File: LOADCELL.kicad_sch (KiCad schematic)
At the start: 11 parts, among them J18 Conn_01x04_Socket, Q4 S8550, U1 HX711

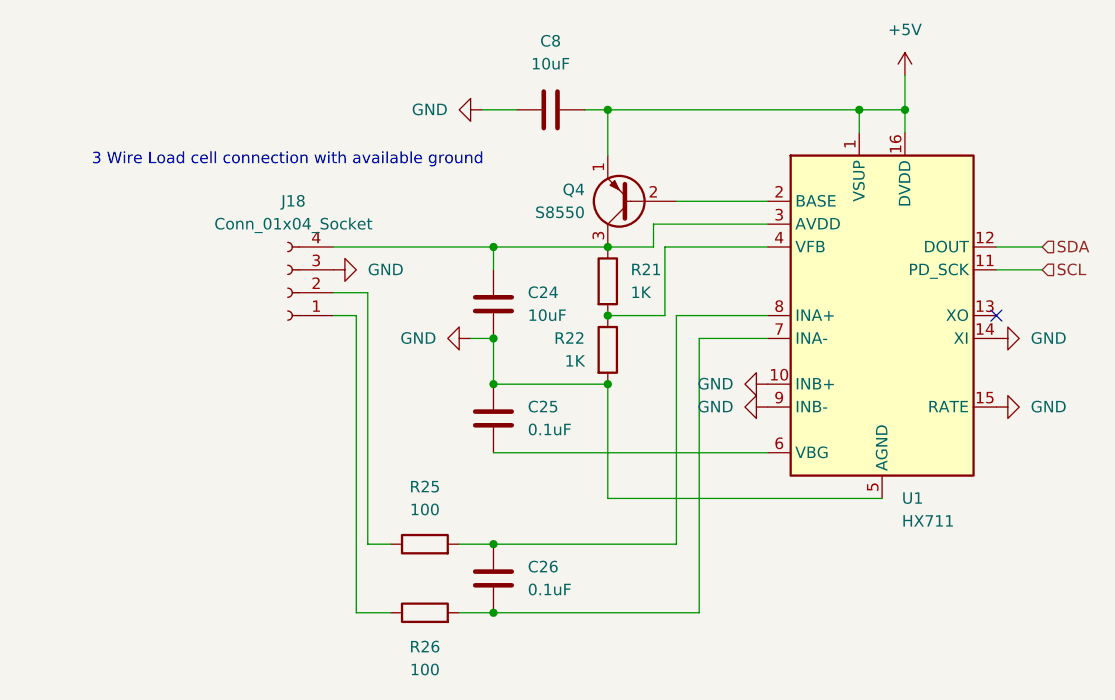
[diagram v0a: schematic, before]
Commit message: progress toward final board, need smaller relays
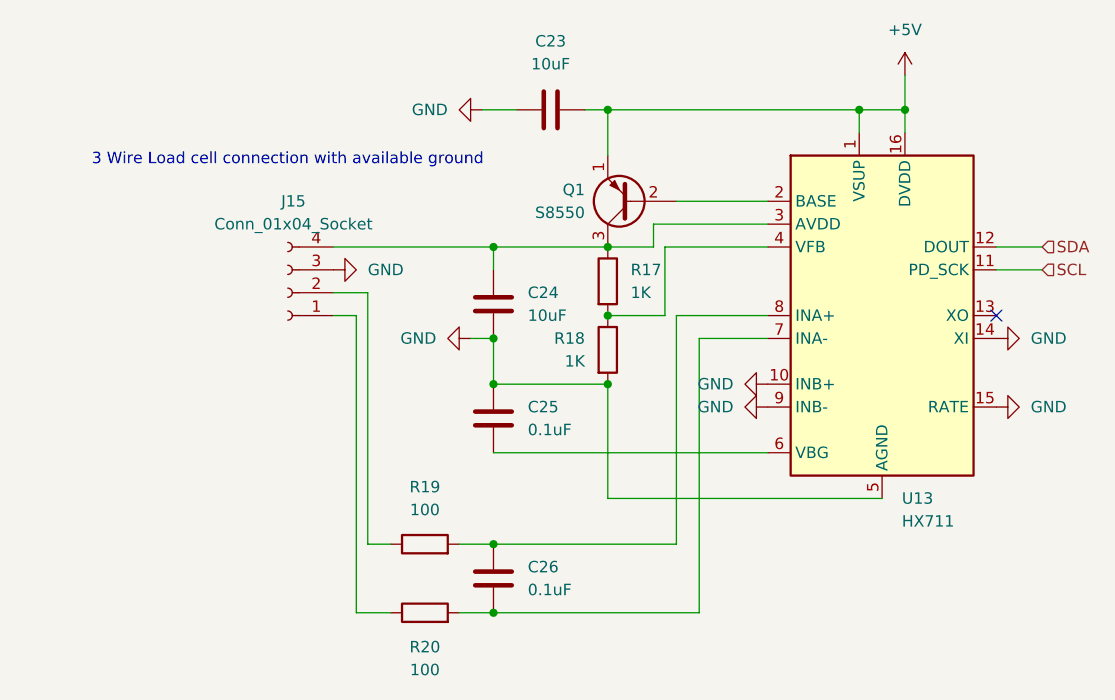
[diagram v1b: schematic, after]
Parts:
- C23: renamed from C8; footprint (none) -> Capacitor_SMD:C_0402_1005Metric
- C24, C25, C26: footprint (none) -> Capacitor_SMD:C_0402_1005Metric
- R17: renamed from R21; footprint (none) -> Resistor_SMD:R_0603_1608Metric
- R18: renamed from R22; footprint (none) -> Resistor_SMD:R_0603_1608Metric
- R19: renamed from R25; footprint (none) -> Resistor_SMD:R_0603_1608Metric
- R20: renamed from R26; footprint (none) -> Resistor_SMD:R_0603_1608Metric
- renumbered J18 to J15, Q4 to Q1, U1 to U13
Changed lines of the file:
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@@
 			)
 		)
-		(property "Footprint" ""
+		(property "Footprint" "Capacitor_SMD:C_0402_1005Metric"
 			(at 56.1848 90.17 0)
 			(effects
@@
 			)
 		)
-		(property "Footprint" ""
+		(property "Footprint" "Capacitor_SMD:C_0402_1005Metric"
 			(at 56.1848 77.47 0)
 			(effects
@@
 		(dnp no)
 		(fields_autoplaced yes)
-		(property "Reference" "C8"
+		(property "Reference" "C23"
 			(at 63.5 52.07 90)
 			(effects
@@
 			)
 		)
-		(property "Footprint" ""
+		(property "Footprint" "Capacitor_SMD:C_0402_1005Metric"
 			(at 67.31 58.7248 0)
 			(effects
@@
 			(project "JAS Warhead PCB"
 				(path "/a037544f-9a20-478c-bac0-d162f9edf245/6ae02261-e46d-4a19-ac1e-bbc1cf38fab0"
-					(reference "C8")
+					(reference "C23")
 					(unit 1)
 				)
@@
 		(dnp no)
 		(fields_autoplaced yes)
-		(property "Reference" "R21"
+		(property "Reference" "R17"
 			(at 72.39 77.4699 0)
 			(effects
@@
 			)
 		)
-		(property "Footprint" ""
+		(property "Footprint" "Resistor_SMD:R_0603_1608Metric"
 			(at 68.072 78.74 90)
 			(effects
@@
 			(project "JAS Warhead PCB"
 				(path "/a037544f-9a20-478c-bac0-d162f9edf245/6ae02261-e46d-4a19-ac1e-bbc1cf38fab0"
-					(reference "R21")
+					(reference "R17")
 					(unit 1)
 				)
@@
 		(dnp no)
 		(fields_autoplaced yes)
-		(property "Reference" "R26"
+		(property "Reference" "R20"
 			(at 49.53 119.38 90)
 			(effects
@@
 			)
 		)
-		(property "Footprint" ""
+		(property "Footprint" "Resistor_SMD:R_0603_1608Metric"
 			(at 49.53 117.348 90)
 			(effects
@@
 			(project "JAS Warhead PCB"
 				(path "/a037544f-9a20-478c-bac0-d162f9edf245/6ae02261-e46d-4a19-ac1e-bbc1cf38fab0"
-					(reference "R26")
+					(reference "R20")
 					(unit 1)
 				)
@@
 		(dnp no)
 		(fields_autoplaced yes)
-		(property "Reference" "R25"
+		(property "Reference" "R19"
 			(at 49.53 101.6 90)
 			(effects
@@
 			)
 		)
-		(property "Footprint" ""
+		(property "Footprint" "Resistor_SMD:R_0603_1608Metric"
 			(at 49.53 109.728 90)
 			(effects
@@
 			(project "JAS Warhead PCB"
 				(path "/a037544f-9a20-478c-bac0-d162f9edf245/6ae02261-e46d-4a19-ac1e-bbc1cf38fab0"
-					(reference "R25")
+					(reference "R19")
 					(unit 1)
 				)
@@
 		(dnp no)
 		(fields_autoplaced yes)
-		(property "Reference" "J18"
+		(property "Reference" "J15"
 			(at 34.925 69.85 0)
 			(effects
@@
 			(project "JAS Warhead PCB"
 				(path "/a037544f-9a20-478c-bac0-d162f9edf245/6ae02261-e46d-4a19-ac1e-bbc1cf38fab0"
-					(reference "J18")
+					(reference "J15")
 					(unit 1)
 				)
@@
 		(dnp no)
 		(fields_autoplaced yes)
-		(property "Reference" "Q4"
+		(property "Reference" "Q1"
 			(at 67.31 68.5799 0)
 			(effects
@@
 			(project "JAS Warhead PCB"
 				(path "/a037544f-9a20-478c-bac0-d162f9edf245/6ae02261-e46d-4a19-ac1e-bbc1cf38fab0"
-					(reference "Q4")
+					(reference "Q1")
 					(unit 1)
 				)
@@
 			)
 		)
-		(property "Footprint" ""
+		(property "Footprint" "Capacitor_SMD:C_0402_1005Metric"
 			(at 56.1848 107.95 0)
 			(effects
@@
 		(dnp no)
 		(fields_autoplaced yes)
-		(property "Reference" "#PWR076"
+		(property "Reference" "#PWR074"
 			(at 49.53 59.69 0)
 			(effects
@@
 			(project "JAS Warhead PCB"
 				(path "/a037544f-9a20-478c-bac0-d162f9edf245/6ae02261-e46d-4a19-ac1e-bbc1cf38fab0"
-					(reference "#PWR076")
+					(reference "#PWR074")
 					(unit 1)
 				)
@@
 		(dnp no)
 		(fields_autoplaced yes)
-		(property "Reference" "#PWR082"
+		(property "Reference" "#PWR075"
 			(at 45.72 77.47 0)
 			(effects
@@
 			(project "JAS Warhead PCB"
 				(path "/a037544f-9a20-478c-bac0-d162f9edf245/6ae02261-e46d-4a19-ac1e-bbc1cf38fab0"
-					(reference "#PWR082")
+					(reference "#PWR075")
 					(unit 1)
 				)
@@
 		(dnp no)
 		(fields_autoplaced yes)
-		(property "Reference" "#PWR081"
+		(property "Reference" "#PWR077"
 			(at 119.38 85.09 0)
 			(effects
@@
 			(project "JAS Warhead PCB"
 				(path "/a037544f-9a20-478c-bac0-d162f9edf245/6ae02261-e46d-4a19-ac1e-bbc1cf38fab0"
-					(reference "#PWR081")
+					(reference "#PWR077")
 					(unit 1)
 				)
@@
 		(dnp no)
 		(fields_autoplaced yes)
-		(property "Reference" "#PWR083"
+		(property "Reference" "#PWR076"
 			(at 48.26 85.09 0)
 			(effects
@@
 			(project "JAS Warhead PCB"
 				(path "/a037544f-9a20-478c-bac0-d162f9edf245/6ae02261-e46d-4a19-ac1e-bbc1cf38fab0"
-					(reference "#PWR083")
+					(reference "#PWR076")
 					(unit 1)
 				)
@@
 		(dnp no)
 		(fields_autoplaced yes)
-		(property "Reference" "R22"
+		(property "Reference" "R18"
 			(at 67.31 85.0899 0)
 			(effects
@@
 			)
 		)
-		(property "Footprint" ""
+		(property "Footprint" "Resistor_SMD:R_0603_1608Metric"
 			(at 68.072 86.36 90)
 			(effects
@@
 			(project "JAS Warhead PCB"
 				(path "/a037544f-9a20-478c-bac0-d162f9edf245/6ae02261-e46d-4a19-ac1e-bbc1cf38fab0"
-					(reference "R22")
+					(reference "R18")
 					(unit 1)
 				)
@@
 		(dnp no)
 		(fields_autoplaced yes)
-		(property "Reference" "U1"
+		(property "Reference" "U13"
 			(at 102.5241 102.87 0)
 			(effects
@@
 			(project "JAS Warhead PCB"
 				(path "/a037544f-9a20-478c-bac0-d162f9edf245/6ae02261-e46d-4a19-ac1e-bbc1cf38fab0"
-					(reference "U1")
+					(reference "U13")
 					(unit 1)
 				)
@@
 		(dnp no)
 		(fields_autoplaced yes)
-		(property "Reference" "#PWR077"
+		(property "Reference" "#PWR073"
 			(at 102.87 59.69 0)
 			(effects
@@
 			(project "JAS Warhead PCB"
 				(path "/a037544f-9a20-478c-bac0-d162f9edf245/6ae02261-e46d-4a19-ac1e-bbc1cf38fab0"
-					(reference "#PWR077")
-					(unit 1)
-				)
+					(reference "#PWR073")
+					(unit 1)
+				)

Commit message: almost there
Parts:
- removed Q1: S8550, Package_TO_SOT_THT:TO-92_Inline, symbol Transistor_BJT:S8550
- added Q2: S8550M-D, blastLib:SOT-23-3_L2.9-W1.6-P1.90-LS2.8-BR, symbol blastLib:S8550M-D
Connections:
- net at C24.2, J15.4 (Pin_4), R17.1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: now also Q2.3 (C)
- net at R20.1: now also J15.2 (Pin_2); no longer J15.1 (Pin_1)
- net at R19.1: now also J15.1 (Pin_1); no longer J15.2 (Pin_2)
- net at U13.2 (BASE): now also Q2.1 (B)
- net +5V renamed +3V3
- net +3V3: now also Q2.2 (E)
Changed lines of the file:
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@@
+	)
+	(junction
+		(at 102.87 59.69)
+		(diameter 0)
+		(color 0 0 0 0)
 	)
 	(junction
@@
 	)
 	(junction
-		(at 102.87 59.69)
-		(diameter 0)
-		(color 0 0 0 0)
-	)
-	(junction
 		(at 57.15 74.93)
 		(diameter 0)
@@
 	(wire
 		(pts
+			(xy 41.91 80.01) (xy 41.91 115.57)
+		)
+		(stroke
+			(width 0)
+			(type default)
+		)
+	)
+	(wire
+		(pts
 			(xy 57.15 115.57) (xy 80.01 115.57)
 		)
@@
 	(wire
 		(pts
-			(xy 102.87 55.88) (xy 102.87 59.69)
-		)
-		(stroke
-			(width 0)
-			(type default)
-		)
-	)
-	(wire
-		(pts
 			(xy 118.11 74.93) (xy 113.03 74.93)
 		)
@@
 	(wire
 		(pts
-			(xy 43.18 107.95) (xy 43.18 80.01)
-		)
-		(stroke
-			(width 0)
-			(type default)
-		)
-	)
-	(wire
-		(pts
 			(xy 76.2 82.55) (xy 69.85 82.55)
 		)
@@
 	(wire
 		(pts
+			(xy 74.93 69.85) (xy 87.63 69.85)
+		)
+		(stroke
+			(width 0)
+			(type default)
+		)
+	)
+	(wire
+		(pts
 			(xy 57.15 107.95) (xy 77.47 107.95)
 		)
@@
 	(wire
 		(pts
-			(xy 43.18 80.01) (xy 39.37 80.01)
-		)
-		(stroke
-			(width 0)
-			(type default)
-		)
-	)
-	(wire
-		(pts
-			(xy 45.72 107.95) (xy 43.18 107.95)
+			(xy 40.64 107.95) (xy 45.72 107.95)
 		)
 		(stroke
@@
 	(wire
 		(pts
+			(xy 41.91 80.01) (xy 39.37 80.01)
+		)
+		(stroke
+			(width 0)
+			(type default)
+		)
+	)
+	(wire
+		(pts
 			(xy 77.47 82.55) (xy 77.47 107.95)
 		)
@@
 	(wire
 		(pts
+			(xy 40.64 82.55) (xy 39.37 82.55)
+		)
+		(stroke
+			(width 0)
+			(type default)
+		)
+	)
+	(wire
+		(pts
 			(xy 87.63 82.55) (xy 77.47 82.55)
 		)
@@
 	(wire
 		(pts
-			(xy 77.47 69.85) (xy 87.63 69.85)
-		)
-		(stroke
-			(width 0)
-			(type default)
-		)
-	)
-	(wire
-		(pts
 			(xy 74.93 72.39) (xy 74.93 74.93)
 		)
@@
 	(wire
 		(pts
-			(xy 41.91 82.55) (xy 39.37 82.55)
+			(xy 40.64 107.95) (xy 40.64 82.55)
 		)
 		(stroke
@@
 		(pts
 			(xy 118.11 77.47) (xy 113.03 77.47)
-		)
-		(stroke
-			(width 0)
-			(type default)
-		)
-	)
-	(wire
-		(pts
-			(xy 41.91 115.57) (xy 41.91 82.55)
 		)
 		(stroke
@@
 	)
 	(symbol
+		(lib_id "power:+3V3")
+		(at 102.87 59.69 0)
+		(unit 1)
+		(exclude_from_sim no)
+		(in_bom yes)
+		(on_board yes)
+		(dnp no)
+		(property "Reference" "#PWR048"
+			(at 102.87 63.5 0)
+			(effects
+				(font
+					(size 1.27 1.27)
+				)
+				(hide yes)
+			)
+		)
+		(property "Value" "+3V3"
+			(at 102.87 56.134 0)
+			(effects
+				(font
+					(size 1.27 1.27)
+				)
+			)
+		)
+		(property "Footprint" ""
+			(at 102.87 59.69 0)
+			(effects
+				(font
+					(size 1.27 1.27)
+				)
+				(hide yes)
+			)
+		)
+		(property "Datasheet" ""
+			(at 102.87 59.69 0)
+			(effects
+				(font
+					(size 1.27 1.27)
+				)
+				(hide yes)
+			)
+		)
+		(property "Description" "Power symbol creates a global label with name \"+3V3\""
+			(at 102.87 59.69 0)
+			(effects
+				(font
+					(size 1.27 1.27)
+				)
+				(hide yes)
+			)
+		)
+		(pin "1"
+		)
+		(instances
+			(project "JAS Warhead PCB"
+				(path "/a037544f-9a20-478c-bac0-d162f9edf245/6ae02261-e46d-4a19-ac1e-bbc1cf38fab0"
+					(reference "#PWR048")
+					(unit 1)
+				)
+			)
+		)
+	)
+	(symbol
 		(lib_id "power:GND")
 		(at 87.63 92.71 270)
@@
 	)
 	(symbol
-		(lib_id "Transistor_BJT:S8550")
-		(at 72.39 69.85 180)
-		(unit 1)
-		(exclude_from_sim no)
-		(in_bom yes)
-		(on_board yes)
-		(dnp no)
-		(fields_autoplaced yes)
-		(property "Reference" "Q1"
-			(at 67.31 68.5799 0)
-			(effects
-				(font
-					(size 1.27 1.27)
-				)
-				(justify left)
-			)
-		)
-		(property "Value" "S8550"
-			(at 67.31 71.1199 0)
-			(effects
-				(font
-					(size 1.27 1.27)
-				)
-				(justify left)
-			)
-		)
-		(property "Footprint" "Package_TO_SOT_THT:TO-92_Inline"
-			(at 67.31 67.945 0)
-			(effects
-				(font
-					(size 1.27 1.27)
-					(italic yes)
-				)
-				(justify left)
-				(hide yes)
-			)
-		)
-		(property "Datasheet" "http://www.unisonic.com.tw/datasheet/S8550.pdf"
-			(at 72.39 69.85 0)
-			(effects
-				(font
-					(size 1.27 1.27)
-				)
-				(justify left)
-				(hide yes)
-			)
-		)
-		(property "Description" "0.7A Ic, 20V Vce, Low Voltage High Current PNP Transistor, TO-92"
-			(at 72.39 69.85 0)
-			(effects
-				(font
-					(size 1.27 1.27)
-				)
-				(hide yes)
-			)
-		)
-		(pin "3"
-		)
-		(pin "1"
-		)
-		(pin "2"
-		)
-		(instances
-			(project "JAS Warhead PCB"
-				(path "/a037544f-9a20-478c-bac0-d162f9edf245/6ae02261-e46d-4a19-ac1e-bbc1cf38fab0"
-					(reference "Q1")
-					(unit 1)
-				)
-			)
-		)
-	)
-	(symbol
 		(lib_id "Device:C")
 		(at 57.15 111.76 180)
@@
 	)
 	(symbol
-		(lib_id "power:+5V")
-		(at 102.87 55.88 0)
-		(unit 1)
-		(exclude_from_sim no)
-		(in_bom yes)
-		(on_board yes)
-		(dnp no)
-		(fields_autoplaced yes)
-		(property "Reference" "#PWR073"
-			(at 102.87 59.69 0)
-			(effects
-				(font
-					(size 1.27 1.27)
-				)
-				(hide yes)
-			)
-		)
-		(property "Value" "+5V"
-			(at 102.87 50.8 0)
-			(effects
-				(font
-					(size 1.27 1.27)
-				)
-			)
-		)
-		(property "Footprint" ""
-			(at 102.87 55.88 0)
-			(effects
-				(font
-					(size 1.27 1.27)
-				)
-				(hide yes)
-			)
-		)
-		(property "Datasheet" ""
-			(at 102.87 55.88 0)
-			(effects
-				(font
-					(size 1.27 1.27)
-				)
-				(hide yes)
-			)
-		)
-		(property "Description" "Power symbol creates a global label with name \"+5V\""
-			(at 102.87 55.88 0)
-			(effects
-				(font
-					(size 1.27 1.27)
-				)
-				(hide yes)
-			)
-		)
-		(pin "1"
-		)
-		(instances
-			(project "JAS Warhead PCB"
-				(path "/a037544f-9a20-478c-bac0-d162f9edf245/6ae02261-e46d-4a19-ac1e-bbc1cf38fab0"
-					(reference "#PWR073")
-					(unit 1)
-				)
+		(lib_id "blastLib:S8550M-D")
+		(at 72.39 69.85 180)
+		(unit 1)
+		(exclude_from_sim no)
+		(in_bom yes)
+		(on_board yes)
+		(dnp no)
+		(fields_autoplaced yes)
+		(property "Reference" "Q2"
+			(at 68.58 68.5799 0)
+			(effects
+				(font
+					(size 1.27 1.27)
+				)
+				(justify left)
+			)
+		)
+		(property "Value" "S8550M-D"
+			(at 68.58 71.1199 0)
+			(effects
+				(font
+					(size 1.27 1.27)
+				)
+				(justify left)
+			)
+		)
+		(property "Footprint" "blastLib:SOT-23-3_L2.9-W1.6-P1.90-LS2.8-BR"
+			(at 72.39 57.15 0)
+			(effects
+				(font
+					(size 1.27 1.27)
+				)
+				(hide yes)
+			)
+		)
+		(property "Datasheet" "https://lcsc.com/product-detail/Transistors-NPN-PNP_BLUE-ROCKET-S8550M-D_C305484.html"
+			(at 72.39 54.61 0)
+			(effects
+				(font
+					(size 1.27 1.27)
+				)
+				(hide yes)
+			)
+		)
+		(property "Description" ""
+			(at 72.39 69.85 0)
+			(effects
+				(font
+					(size 1.27 1.27)
+				)
+				(hide yes)
+			)
+		)
+		(property "LCSC Part" "C305484"
+			(at 72.39 52.07 0)
+			(effects
+				(font
+					(size 1.27 1.27)
+				)
+				(hide yes)
+			)
+		)
+		(pin "1"
+		)
+		(pin "3"
+		)
+		(pin "2"
+		)
+		(instances
+			(project ""
+				(path "/a037544f-9a20-478c-bac0-d162f9edf245/6ae02261-e46d-4a19-ac1e-bbc1cf38fab0"
+					(reference "Q2")
+					(unit 1)
+				)

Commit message: almost ready for prod
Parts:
- C25: value 0.1uF -> 100nF
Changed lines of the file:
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@@
 			)
 		)
-		(property "Value" "0.1uF"
+		(property "Value" "100nF"
 			(at 60.96 95.2499 0)
 			(effects
